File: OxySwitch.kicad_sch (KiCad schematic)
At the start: 0 parts

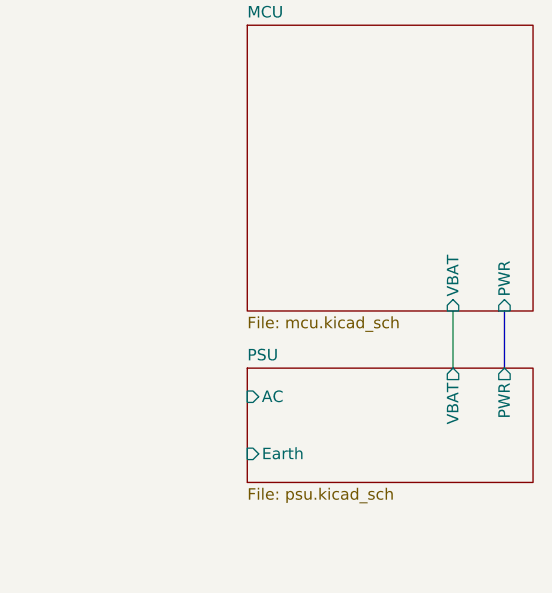
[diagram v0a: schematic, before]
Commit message: Added connectors
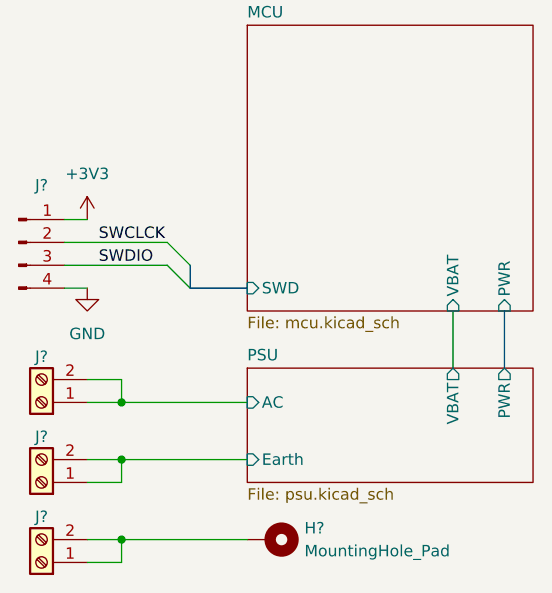
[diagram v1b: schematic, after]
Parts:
- added H?: MountingHole_Pad, symbol Mechanical:MountingHole_Pad
- added J?: Conn_01x04_Male, symbol Connector:Conn_01x04_Male
- added J? (x3): Screw_Terminal_01x02, symbol Connector:Screw_Terminal_01x02
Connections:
- net PSU/AC: now also J?.1 (Pin_1), J?.2 (Pin_2)
- net PSU/Earth: now also J?.1 (Pin_1), J?.2 (Pin_2)
- new net: H?.1, J?.1 (Pin_1), J?.2 (Pin_2)
- new net +3V3: J?.1 (Pin_1)
- new net GND: J?.4 (Pin_4)
- new net SWCLCK: J?.2 (Pin_2)
- new net SWDIO: J?.3 (Pin_3)
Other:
- sheet MCU ports: added SWD; removed none
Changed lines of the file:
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@@
     (company "Tomas Kysela")
   )
+  (junction (at 119.38 137.16) (diameter 0) (color 0 0 0 0)
+  )
+  (junction (at 119.38 143.51) (diameter 0) (color 0 0 0 0)
+  )
+  (junction (at 119.38 152.4) (diameter 0) (color 0 0 0 0)
+  )
+  (bus_entry (at 124.46 119.38) (size 2.54 2.54)
+    (stroke (width 0) (type default) (color 0 0 0 0))
+  )
+  (bus_entry (at 124.46 121.92) (size 2.54 2.54)
+    (stroke (width 0) (type default) (color 0 0 0 0))
+  )
+  (wire (pts (xy 119.38 152.4) (xy 119.38 154.94))
+    (stroke (width 0) (type default) (color 0 0 0 0))
+  )
+  (wire (pts (xy 115.57 146.05) (xy 119.38 146.05))
+    (stroke (width 0) (type default) (color 0 0 0 0))
+  )
+  (wire (pts (xy 119.38 146.05) (xy 119.38 143.51))
+    (stroke (width 0) (type default) (color 0 0 0 0))
+  )
+  (wire (pts (xy 115.57 143.51) (xy 119.38 143.51))
+    (stroke (width 0) (type default) (color 0 0 0 0))
+  )
+  (wire (pts (xy 119.38 137.16) (xy 133.35 137.16))
+    (stroke (width 0) (type default) (color 0 0 0 0))
+  )
+  (wire (pts (xy 119.38 143.51) (xy 133.35 143.51))
+    (stroke (width 0) (type default) (color 0 0 0 0))
+  )
+  (wire (pts (xy 119.38 152.4) (xy 133.35 152.4))
+    (stroke (width 0) (type default) (color 0 0 0 0))
+  )
+  (wire (pts (xy 115.57 152.4) (xy 119.38 152.4))
+    (stroke (width 0) (type default) (color 0 0 0 0))
+  )
+  (wire (pts (xy 115.57 137.16) (xy 119.38 137.16))
+    (stroke (width 0) (type default) (color 0 0 0 0))
+  )
+  (wire (pts (xy 115.57 134.62) (xy 119.38 134.62))
+    (stroke (width 0) (type default) (color 0 0 0 0))
+  )
   (bus (pts (xy 161.925 127) (xy 161.925 133.35))
     (stroke (width 0) (type default) (color 0 0 0 0))
   )
+  (wire (pts (xy 113.03 119.38) (xy 124.46 119.38))
+    (stroke (width 0) (type default) (color 0 0 0 0))
+  )
+  (wire (pts (xy 113.03 121.92) (xy 124.46 121.92))
+    (stroke (width 0) (type default) (color 0 0 0 0))
+  )
   (wire (pts (xy 156.21 127) (xy 156.21 133.35))
     (stroke (width 0) (type default) (color 0 0 0 0))
+  )
+  (wire (pts (xy 113.03 116.84) (xy 115.57 116.84))
+    (stroke (width 0) (type default) (color 0 0 0 0))
+  )
+  (bus (pts (xy 127 121.92) (xy 127 124.46))
+    (stroke (width 0) (type default) (color 0 0 0 0))
+  )
+  (bus (pts (xy 127 124.46) (xy 133.35 124.46))
+    (stroke (width 0) (type default) (color 0 0 0 0))
+  )
+  (wire (pts (xy 115.57 154.94) (xy 119.38 154.94))
+    (stroke (width 0) (type default) (color 0 0 0 0))
+  )
+  (wire (pts (xy 113.03 124.46) (xy 115.57 124.46))
+    (stroke (width 0) (type default) (color 0 0 0 0))
+  )
+  (wire (pts (xy 119.38 134.62) (xy 119.38 137.16))
+    (stroke (width 0) (type default) (color 0 0 0 0))
+  )
+  (label "SWCLCK" (at 116.84 119.38 0)
+    (effects (font (size 1.27 1.27)) (justify left bottom))
+  )
+  (label "SWDIO" (at 116.84 121.92 0)
+    (effects (font (size 1.27 1.27)) (justify left bottom))
+  )
+  (symbol (lib_id "Connector:Conn_01x04_Male") (at 107.95 119.38 0) (unit 1)
+    (in_bom yes) (on_board yes)
+    (property "Reference" "J?" (id 0) (at 110.49 113.03 0))
+    (property "Value" "Conn_01x04_Male" (id 1) (at 106.68 127 0)
+      (effects (font (size 1.27 1.27)) hide)
+    )
+    (property "Footprint" "" (id 2) (at 107.95 119.38 0)
+      (effects (font (size 1.27 1.27)) hide)
+    )
+    (property "Datasheet" "~" (id 3) (at 107.95 119.38 0)
+      (effects (font (size 1.27 1.27)) hide)
+    )
+    (pin "1")
+    (pin "2")
+    (pin "3")
+    (pin "4")
+  )
+  (symbol (lib_id "Connector:Screw_Terminal_01x02") (at 110.49 154.94 180) (unit 1)
+    (in_bom yes) (on_board yes)
+    (property "Reference" "J?" (id 0) (at 110.49 149.86 0))
+    (property "Value" "Screw_Terminal_01x02" (id 1) (at 110.49 157.48 0)
+      (effects (font (size 1.27 1.27)) hide)
+    )
+    (property "Footprint" "" (id 2) (at 110.49 154.94 0)
+      (effects (font (size 1.27 1.27)) hide)
+    )
+    (property "Datasheet" "~" (id 3) (at 110.49 154.94 0)
+      (effects (font (size 1.27 1.27)) hide)
+    )
+    (pin "1")
+    (pin "2")
+  )
+  (symbol (lib_id "power:+3V3") (at 115.57 116.84 0) (unit 1)
+    (in_bom yes) (on_board yes) (fields_autoplaced)
+    (property "Reference" "#PWR?" (id 0) (at 115.57 120.65 0)
+      (effects (font (size 1.27 1.27)) hide)
+    )
+    (property "Value" "+3V3" (id 1) (at 115.57 111.76 0))
+    (property "Footprint" "" (id 2) (at 115.57 116.84 0)
+      (effects (font (size 1.27 1.27)) hide)
+    )
+    (property "Datasheet" "" (id 3) (at 115.57 116.84 0)
+      (effects (font (size 1.27 1.27)) hide)
+    )
+    (pin "1")
+  )
+  (symbol (lib_id "power:GND") (at 115.57 124.46 0) (unit 1)
+    (in_bom yes) (on_board yes) (fields_autoplaced)
+    (property "Reference" "#PWR?" (id 0) (at 115.57 130.81 0)
+      (effects (font (size 1.27 1.27)) hide)
+    )
+    (property "Value" "GND" (id 1) (at 115.57 129.54 0))
+    (property "Footprint" "" (id 2) (at 115.57 124.46 0)
+      (effects (font (size 1.27 1.27)) hide)
+    )
+    (property "Datasheet" "" (id 3) (at 115.57 124.46 0)
+      (effects (font (size 1.27 1.27)) hide)
+    )
+    (pin "1")
+  )
+  (symbol (lib_id "Mechanical:MountingHole_Pad") (at 135.89 152.4 270) (unit 1)
+    (in_bom yes) (on_board yes) (fields_autoplaced)
+    (property "Reference" "H?" (id 0) (at 139.7 151.1299 90)
+      (effects (font (size 1.27 1.27)) (justify left))
+    )
+    (property "Value" "MountingHole_Pad" (id 1) (at 139.7 153.6699 90)
+      (effects (font (size 1.27 1.27)) (justify left))
+    )
+    (property "Footprint" "" (id 2) (at 135.89 152.4 0)
+      (effects (font (size 1.27 1.27)) hide)
+    )
+    (property "Datasheet" "~" (id 3) (at 135.89 152.4 0)
+      (effects (font (size 1.27 1.27)) hide)
+    )
+    (pin "1")
+  )
+  (symbol (lib_id "Connector:Screw_Terminal_01x02") (at 110.49 146.05 180) (unit 1)
+    (in_bom yes) (on_board yes)
+    (property "Reference" "J?" (id 0) (at 110.49 140.97 0))
+    (property "Value" "Screw_Terminal_01x02" (id 1) (at 110.49 148.59 0)
+      (effects (font (size 1.27 1.27)) hide)
+    )
+    (property "Footprint" "" (id 2) (at 110.49 146.05 0)
+      (effects (font (size 1.27 1.27)) hide)
+    )
+    (property "Datasheet" "~" (id 3) (at 110.49 146.05 0)
+      (effects (font (size 1.27 1.27)) hide)
+    )
+    (pin "1")
+    (pin "2")
+  )
+  (symbol (lib_id "Connector:Screw_Terminal_01x02") (at 110.49 137.16 180) (unit 1)
+    (in_bom yes) (on_board yes)
+    (property "Reference" "J?" (id 0) (at 110.49 132.08 0))
+    (property "Value" "Screw_Terminal_01x02" (id 1) (at 110.49 139.7 0)
+      (effects (font (size 1.27 1.27)) hide)
+    )
+    (property "Footprint" "" (id 2) (at 110.49 137.16 0)
+      (effects (font (size 1.27 1.27)) hide)
+    )
+    (property "Datasheet" "~" (id 3) (at 110.49 137.16 0)
+      (effects (font (size 1.27 1.27)) hide)
+    )
+    (pin "1")
+    (pin "2")
   )
   (sheet (at 133.35 133.35) (size 31.75 12.7) (fields_autoplaced)
@@
       (effects (font (size 1.27 1.27)) (justify left top))
     )
-    (pin "AC" input (at 133.35 136.525 180)
-      (effects (font (size 1.27 1.27)) (justify left))
-    )
-    (pin "Earth" input (at 133.35 142.875 180)
+    (pin "AC" input (at 133.35 137.16 180)
+      (effects (font (size 1.27 1.27)) (justify left))
+    )
+    (pin "Earth" input (at 133.35 143.51 180)
       (effects (font (size 1.27 1.27)) (justify left))
     )
@@
       (effects (font (size 1.27 1.27)) (justify left))
     )
+    (pin "SWD" input (at 133.35 124.46 180)
+      (effects (font (size 1.27 1.27)) (justify left))
+    )
   )
   (sheet_instances
@@
       (reference "#PWR?") (unit 1) (value "GND") (footprint "")
     )
+    (path "/13fffc85-30de-4241-8ace-b7305ede4b0f"
+      (reference "#PWR?") (unit 1) (value "+3V3") (footprint "")
+    )
     (path "/13cf60ac-65e2-4c08-a52d-012b34ab8e81/16c516ac-cb48-42fc-8edd-7004fbe5bce7"
       (reference "#PWR?") (unit 1) (value "GND") (footprint "")
@@
     )
     (path "/f0a48b94-eb9d-48cd-8f5c-0b4d1593339f/259540bc-7932-43ed-b8bf-5e1ee9ece529"
+      (reference "#PWR?") (unit 1) (value "GND") (footprint "")
+    )
+    (path "/2b20f2df-aed2-4951-a1d6-eade8d9f7825"
       (reference "#PWR?") (unit 1) (value "GND") (footprint "")
     )
@@
       (reference "#PWR?") (unit 1) (value "GND") (footprint "")
     )
+    (path "/13cf60ac-65e2-4c08-a52d-012b34ab8e81/4fbc7894-a927-482f-8538-4a4e2d8b7014"
+      (reference "#PWR?") (unit 1) (value "+3V3") (footprint "")
+    )
     (path "/f0a48b94-eb9d-48cd-8f5c-0b4d1593339f/774c6cf0-8f81-4158-afa1-ad665afae4f0"
       (reference "#PWR?") (unit 1) (value "GND") (footprint "")
@@
       (reference "C?") (unit 1) (value "4u7") (footprint "")
     )
+    (path "/64f5bc87-6d55-4a37-be30-6f754a68da27"
+      (reference "H?") (unit 1) (value "MountingHole_Pad") (footprint "")
+    )
     (path "/f0a48b94-eb9d-48cd-8f5c-0b4d1593339f/361efe96-e010-460b-9ab1-352e91084e16"
       (reference "IC?") (unit 1) (value "STM32WB35CEU6A") (footprint "OxySwitch:STM32WB35CEU6A")
@@
       (reference "IC?") (unit 1) (value "BD33IA5WEFJ-E2") (footprint "SOIC127P600X100-9N")
     )
+    (path "/02eb0d5a-7331-4d4a-8634-180a7d427871"
+      (reference "J?") (unit 1) (value "Conn_01x04_Male") (footprint "")
+    )
+    (path "/07165ece-1d03-4ed1-9909-d45e23198e5f"
+      (reference "J?") (unit 1) (value "Screw_Terminal_01x02") (footprint "")
+    )
+    (path "/97796805-3d35-4565-873d-fe151e7ccdb0"
+      (reference "J?") (unit 1) (value "Screw_Terminal_01x02") (footprint "")
+    )
+    (path "/caa9825f-7856-4868-96be-7a752caada7d"
+      (reference "J?") (unit 1) (value "Screw_Terminal_01x02") (footprint "")
+    )
     (path "/f0a48b94-eb9d-48cd-8f5c-0b4d1593339f/3004af65-c156-450e-9651-bfddc2af78b3"

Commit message: Added RF
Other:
- added sheet RF (rf.kicad_sch)
- sheet MCU ports: added RF1; removed none
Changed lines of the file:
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@@
+    )
+  )
+  (sheet (at 177.8 95.25) (size 22.86 31.75) (fields_autoplaced)
+    (stroke (width 0.1524) (type solid) (color 0 0 0 0))
+    (fill (color 0 0 0 0.0000))
+    (property "Sheet name" "RF" (id 0) (at 177.8 94.5384 0)
+      (effects (font (size 1.27 1.27)) (justify left bottom))
+    )
+    (property "Sheet file" "rf.kicad_sch" (id 1) (at 177.8 127.5846 0)
+      (effects (font (size 1.27 1.27)) (justify left top))
     )
   )
@@
       (effects (font (size 1.27 1.27)) (justify left))
     )
+    (pin "RF1" input (at 165.1 118.11 0)
+      (effects (font (size 1.27 1.27)) (justify right))
+    )
   )
   (sheet_instances
@@
     (path "/13cf60ac-65e2-4c08-a52d-012b34ab8e81" (page "3"))
     (path "/13cf60ac-65e2-4c08-a52d-012b34ab8e81/328173b0-1baf-4f2c-ac09-4ab7a43064f8" (page "4"))
+    (path "/e23d2dad-3518-4617-9254-596253535c35" (page "5"))
   )
   (symbol_instances
@@
       (reference "#PWR?") (unit 1) (value "GND") (footprint "")
     )
+    (path "/e23d2dad-3518-4617-9254-596253535c35/185d3052-c68e-495c-a456-ea48a185dc04"
+      (reference "#PWR?") (unit 1) (value "GND") (footprint "")
+    )
     (path "/13cf60ac-65e2-4c08-a52d-012b34ab8e81/244d6c86-5a07-48a3-9fb2-9cdca80de620"
       (reference "#PWR?") (unit 1) (value "GND") (footprint "")
@@
     )
     (path "/2b20f2df-aed2-4951-a1d6-eade8d9f7825"
+      (reference "#PWR?") (unit 1) (value "GND") (footprint "")
+    )
+    (path "/e23d2dad-3518-4617-9254-596253535c35/3483c0d6-bddb-40c2-842d-a7bcf7a3676f"
       (reference "#PWR?") (unit 1) (value "GND") (footprint "")
     )
@@
       (reference "#PWR?") (unit 1) (value "+3V3") (footprint "")
     )
+    (path "/e23d2dad-3518-4617-9254-596253535c35/53f8b603-97f8-4874-890a-d4fb0f9a7222"
+      (reference "#PWR?") (unit 1) (value "GND") (footprint "")
+    )
     (path "/f0a48b94-eb9d-48cd-8f5c-0b4d1593339f/774c6cf0-8f81-4158-afa1-ad665afae4f0"
       (reference "#PWR?") (unit 1) (value "GND") (footprint "")
@@
       (reference "#PWR?") (unit 1) (value "GND") (footprint "")
     )
+    (path "/e23d2dad-3518-4617-9254-596253535c35/a67d30b5-b258-4972-ac9d-34c50a925cb7"
+      (reference "#PWR?") (unit 1) (value "GND") (footprint "")
+    )
     (path "/f0a48b94-eb9d-48cd-8f5c-0b4d1593339f/a9320bc6-b6ff-4cb9-8399-d09a4a343d13"
       (reference "#PWR?") (unit 1) (value "GND") (footprint "")
@@
       (reference "#PWR?") (unit 1) (value "GND") (footprint "")
     )
+    (path "/e23d2dad-3518-4617-9254-596253535c35/c143a1e4-ebdd-4a6f-9059-8e99296414ef"
+      (reference "#PWR?") (unit 1) (value "GND") (footprint "")
+    )
     (path "/f0a48b94-eb9d-48cd-8f5c-0b4d1593339f/d2314796-4533-40c9-ab04-698b2bd28c7f"
       (reference "#PWR?") (unit 1) (value "GND") (footprint "")
@@
       (reference "#PWR?") (unit 1) (value "GND") (footprint "")
     )
+    (path "/e23d2dad-3518-4617-9254-596253535c35/f2c83cd5-f6d1-4b92-894c-57334786e9b4"
+      (reference "#PWR?") (unit 1) (value "GND") (footprint "")
+    )
     (path "/13cf60ac-65e2-4c08-a52d-012b34ab8e81/f8632439-093d-4508-83fa-1d30e75a17af"
       (reference "#PWR?") (unit 1) (value "GND") (footprint "")
@@
     (path "/f0a48b94-eb9d-48cd-8f5c-0b4d1593339f/f8829b90-ef76-40ff-9b9c-80358331a69c"
       (reference "#PWR?") (unit 1) (value "GND") (footprint "")
+    )
+    (path "/e23d2dad-3518-4617-9254-596253535c35/27732b14-f163-4169-9b2b-157433c473ae"
+      (reference "ANT?") (unit 1) (value "ANT3216LL00R2400A") (footprint "ANT3216LL00R2400A")
     )
     (path "/13cf60ac-65e2-4c08-a52d-012b34ab8e81/328173b0-1baf-4f2c-ac09-4ab7a43064f8/ca430ff8-05d7-4562-b0d0-f94e599ede35"
@@
       (reference "C?") (unit 1) (value "100n") (footprint "")
     )
+    (path "/e23d2dad-3518-4617-9254-596253535c35/6c38ef7b-6ca9-476b-b38a-558e722ee147"
+      (reference "C?") (unit 1) (value "0p3") (footprint "")
+    )
     (path "/13cf60ac-65e2-4c08-a52d-012b34ab8e81/9ef3806e-a7d1-4b3b-91fd-60df0556741e"
       (reference "C?") (unit 1) (value "4u7") (footprint "")
@@
       (reference "C?") (unit 1) (value "C") (footprint "")
     )
+    (path "/e23d2dad-3518-4617-9254-596253535c35/a6d00c2c-0a4f-4fb6-88ab-e56ce2c1ed2d"
+      (reference "C?") (unit 1) (value "0p8") (footprint "")
+    )
     (path "/13cf60ac-65e2-4c08-a52d-012b34ab8e81/d68cd8e0-908c-4df6-9777-ccb5a25512ba"
       (reference "C?") (unit 1) (value "10n") (footprint "")
@@
       (reference "C?") (unit 1) (value "4u7") (footprint "")
     )
+    (path "/e23d2dad-3518-4617-9254-596253535c35/5cb7f565-938e-4ed7-8543-3cd57cb741bd"
+      (reference "FL?") (unit 1) (value "748112024") (footprint "748112024")
+    )
     (path "/64f5bc87-6d55-4a37-be30-6f754a68da27"
       (reference "H?") (unit 1) (value "MountingHole_Pad") (footprint "")
@@
       (reference "J?") (unit 1) (value "Screw_Terminal_01x02") (footprint "")
     )
+    (path "/e23d2dad-3518-4617-9254-596253535c35/1f7a1bce-e76e-4ba9-bd82-f0695bdc8e29"
+      (reference "L?") (unit 1) (value "2n7") (footprint "")
+    )
     (path "/f0a48b94-eb9d-48cd-8f5c-0b4d1593339f/3004af65-c156-450e-9651-bfddc2af78b3"

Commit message: Added RF
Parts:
- removed J?: Conn_01x04_Male, symbol Connector:Conn_01x04_Male
- added J?: Conn_ARM_JTAG_SWD_10, symbol Connector:Conn_ARM_JTAG_SWD_10
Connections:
- net +3V3: now also J?.1 (VTref)
- net GND: now also J?.3 (GND), J?.5 (GND), J?.9 (GNDDetect)
- net SWCLCK: now also J?.4 (SWDCLK/TCK)
- net SWDIO: now also J?.2 (SWDIO/TMS)
- new net MCU/NRST: J?.10 (~{RESET})
- no-connect marks 0 -> 2
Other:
- sheet MCU ports: added NRST; removed none
- sheet RF ports: added RF1; removed none

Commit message: ERC
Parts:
- removed H?: MountingHole_Pad, symbol Mechanical:MountingHole_Pad
- added H101: MountingHole_Pad, symbol Mechanical:MountingHole_Pad
- gave numbers to parts that had none: 4
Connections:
- net IN.PE: now reaches J103.1 (Pin_1), J103.2 (Pin_2)
- net IN.PE: now also H101.1
- net PSU/AC renamed IN.L
- net PSU/Earth renamed IN.N
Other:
- sheet MCU ports: added {SWD}, {VDD}; removed PWR, SWD
- sheet PSU ports: added +3V3, IN{PWR}, {VDD}; removed AC, Earth, PWR
- note added: "Case mounting pad"
- note added: "IN PWR terminals"
- moved on the sheet: J101, J102, J103

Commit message: Schematic cleanup
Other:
- sheet PSU ports: added 5V{PWR}; removed none
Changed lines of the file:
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@@
     (stroke (width 0) (type default) (color 0 0 0 0))
   )
+  (bus (pts (xy 123.19 149.225) (xy 133.35 149.225))
+    (stroke (width 0) (type default) (color 0 0 0 0))
+  )
   (text "IN PWR terminals" (at 33.02 196.85 0)
     (effects (font (size 1.27 1.27)) (justify left bottom))
@@
     (effects (font (size 1.27 1.27)) (justify left bottom))
   )
-  (global_label "IN{PWR}" (shape input) (at 40.005 190.5 0) (fields_autoplaced)
+  (global_label "IN{PWR}" (shape output) (at 40.005 190.5 0) (fields_autoplaced)
     (effects (font (size 1.27 1.27)) (justify left))
     (property "Intersheet References" "${INTERSHEET_REFS}" (id 0) (at 50.0381 190.4206 0)
@@
     )
   )
-  (global_label "+3V3" (shape input) (at 123.19 143.51 180) (fields_autoplaced)
+  (global_label "+3V3" (shape output) (at 123.19 143.51 180) (fields_autoplaced)
     (effects (font (size 1.27 1.27)) (justify right))
     (property "Intersheet References" "${INTERSHEET_REFS}" (id 0) (at 115.6969 143.4306 0)
@@
     (effects (font (size 1.27 1.27)) (justify right))
     (property "Intersheet References" "${INTERSHEET_REFS}" (id 0) (at 113.1569 137.2394 0)
+      (effects (font (size 1.27 1.27)) (justify right) hide)
+    )
+  )
+  (global_label "5V{PWR}" (shape output) (at 123.19 149.225 180) (fields_autoplaced)
+    (effects (font (size 1.27 1.27)) (justify right))
+    (property "Intersheet References" "${INTERSHEET_REFS}" (id 0) (at 112.794 149.1456 0)
       (effects (font (size 1.27 1.27)) (justify right) hide)
     )
@@
     )
   )
-  (sheet (at 133.35 133.35) (size 31.75 12.7) (fields_autoplaced)
+  (sheet (at 133.35 133.35) (size 31.75 25.4) (fields_autoplaced)
     (stroke (width 0.1524) (type solid) (color 0 0 0 0))
     (fill (color 0 0 0 0.0000))
@@
       (effects (font (size 1.27 1.27)) (justify left bottom))
     )
-    (property "Sheet file" "psu.kicad_sch" (id 1) (at 133.35 146.6346 0)
+    (property "Sheet file" "psu.kicad_sch" (id 1) (at 133.35 159.3346 0)
       (effects (font (size 1.27 1.27)) (justify left top))
     )
@@
       (effects (font (size 1.27 1.27)) (justify left))
     )
-    (pin "+3V3" input (at 133.35 143.51 180)
+    (pin "+3V3" output (at 133.35 143.51 180)
+      (effects (font (size 1.27 1.27)) (justify left))
+    )
+    (pin "5V{PWR}" output (at 133.35 149.225 180)
       (effects (font (size 1.27 1.27)) (justify left))
     )
@@
       (effects (font (size 1.27 1.27)) (justify left))
     )
-    (pin "RF1" input (at 165.1 114.3 0)
+    (pin "RF1" output (at 165.1 114.3 0)
       (effects (font (size 1.27 1.27)) (justify right))
     )
@@
       (effects (font (size 1.27 1.27)) (justify left))
     )
-    (pin "{SWD}" input (at 132.715 121.92 180)
-      (effects (font (size 1.27 1.27)) (justify left))
-    )
+    (pin "{SWD}" output (at 132.715 121.92 180)
+      (effects (font (size 1.27 1.27)) (justify left))
+    )
